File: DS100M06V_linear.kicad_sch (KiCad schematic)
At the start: 140 parts, among them J1 wire2board, J10 BNC_panel_mount, J11 wire2board, J2 Wire2Board, J3 wire2board, J4 wire2board, J5 Wire2Board, J6 Wire2Board, J7 Wire2Board, J8 red_safety_4mm_connector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

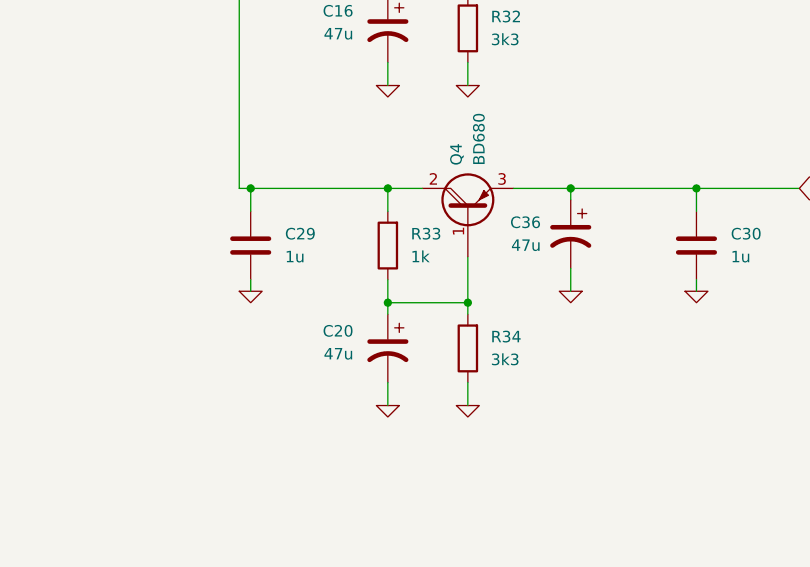
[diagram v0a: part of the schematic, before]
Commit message: Fixed electrolytics.
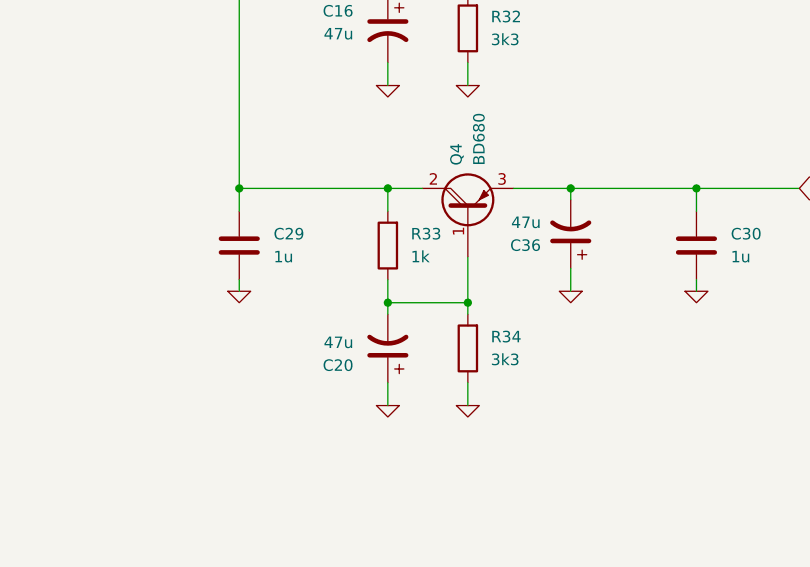
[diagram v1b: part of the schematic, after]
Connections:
- net -5V: now also C36.2; no longer C36.1
- net 0: now also C20.1, C36.1; no longer C20.2, C36.2
- net at Q4.1 (B), R33.1, R34.2: now also C20.2; no longer C20.1
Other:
- moved on the sheet: C20, C29, C36
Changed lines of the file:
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@@
 	)
 	(junction
-		(at 261.62 177.8)
+		(at 331.47 213.36)
 		(diameter 0)
 		(color 0 0 0 0)
 	)
 	(junction
-		(at 332.74 213.36)
+		(at 261.62 177.8)
 		(diameter 0)
 		(color 0 0 0 0)
@@
 	(wire
 		(pts
-			(xy 331.47 213.36) (xy 332.74 213.36)
+			(xy 331.47 213.36) (xy 347.98 213.36)
 		)
 		(stroke
@@
 	(wire
 		(pts
-			(xy 332.74 213.36) (xy 347.98 213.36)
-		)
-		(stroke
-			(width 0)
-			(type default)
-		)
-	)
-	(wire
-		(pts
 			(xy 368.3 189.23) (xy 368.3 186.69)
 		)
@@
 	(wire
 		(pts
-			(xy 332.74 224.79) (xy 332.74 223.52)
+			(xy 331.47 224.79) (xy 331.47 223.52)
 		)
 		(stroke
@@
 	(wire
 		(pts
-			(xy 332.74 213.36) (xy 332.74 215.9)
+			(xy 331.47 213.36) (xy 331.47 215.9)
 		)
 		(stroke
@@
 	(symbol
 		(lib_id "Device:C_Polarized_US")
-		(at 368.3 218.44 0)
-		(mirror y)
+		(at 368.3 218.44 180)
 		(unit 1)
 		(exclude_from_sim no)
@@
 		(dnp no)
 		(property "Reference" "C36"
-			(at 364.998 217.17 0)
+			(at 364.998 219.71 0)
 			(effects
 				(font
@@
 		)
 		(property "Value" "47u"
-			(at 364.998 219.71 0)
+			(at 364.998 217.17 0)
 			(effects
 				(font
@@
 	(symbol
 		(lib_id "Simulation_SPICE:0")
-		(at 332.74 224.79 0)
+		(at 331.47 224.79 0)
 		(unit 1)
 		(exclude_from_sim no)
@@
 		(fields_autoplaced yes)
 		(property "Reference" "#GND030"
-			(at 332.74 227.33 0)
+			(at 331.47 227.33 0)
 			(effects
 				(font
@@
 		)
 		(property "Value" "0"
-			(at 332.74 222.25 0)
+			(at 331.47 222.25 0)
 			(effects
 				(font
@@
 		)
 		(property "Footprint" ""
-			(at 332.74 224.79 0)
+			(at 331.47 224.79 0)
 			(effects
 				(font
@@
 		)
 		(property "Datasheet" "~"
-			(at 332.74 224.79 0)
+			(at 331.47 224.79 0)
 			(effects
 				(font
@@
 		)
 		(property "Description" ""
-			(at 332.74 224.79 0)
+			(at 331.47 224.79 0)
 			(effects
 				(font
@@
 	(symbol
 		(lib_id "Device:C")
-		(at 332.74 219.71 0)
+		(at 331.47 219.71 0)
 		(mirror y)
 		(unit 1)
@@
 		(fields_autoplaced yes)
 		(property "Reference" "C29"
-			(at 336.55 218.44 0)
+			(at 335.28 218.44 0)
 			(effects
 				(font
@@
 		)
 		(property "Value" "1u"
-			(at 336.55 220.98 0)
+			(at 335.28 220.98 0)
 			(effects
 				(font
@@
 		)
 		(property "Footprint" "Resistor_SMD:R_0603_1608Metric_Pad0.98x0.95mm_HandSolder"
-			(at 331.7748 223.52 0)
+			(at 330.5048 223.52 0)
 			(effects
 				(font
@@
 		)
 		(property "Datasheet" "~"
-			(at 332.74 219.71 0)
+			(at 331.47 219.71 0)
 			(effects
 				(font
@@
 		)
 		(property "Description" ""
-			(at 332.74 219.71 0)
+			(at 331.47 219.71 0)
 			(effects
 				(font
@@
 	(symbol
 		(lib_id "Device:C_Polarized_US")
-		(at 347.98 231.14 0)
-		(mirror y)
+		(at 347.98 231.14 180)
 		(unit 1)
 		(exclude_from_sim no)
@@
 		(on_board yes)
 		(dnp no)
-		(fields_autoplaced yes)
 		(property "Reference" "C20"
-			(at 344.17 229.2349 0)
+			(at 344.17 233.0451 0)
 			(effects
 				(font
@@
 		)
 		(property "Value" "47u"
-			(at 344.17 231.7749 0)
+			(at 344.17 230.5051 0)
 			(effects
 				(font

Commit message: Ferrites.
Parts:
- added FB1, FB2, FB3, FB4: FerriteBead, Inductor_SMD:L_0603_1608Metric_Pad1.05x0.95mm_HandSolder, symbol Device:FerriteBead
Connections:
- net +5V: now also FB2.2, FB4.2; no longer C19.2, C21.2, C26.2, C33.2, C34.2, C37.2, U1.8 (V+), U4.7 (V+)
- net -5V: now also FB1.2, FB3.2; no longer C18.2, C22.2, C25.2, C27.2, C35.2, C38.2, U1.4 (V-), U4.4 (V-)
- new net: C22.2, C25.2, C38.2, FB3.1, U4.4 (V-)
- new net: C21.2, C26.2, C37.2, FB4.1, U4.7 (V+)
- new net: C18.2, C27.2, C35.2, FB1.1, U1.4 (V-)
- new net: C19.2, C33.2, C34.2, FB2.1, U1.8 (V+)
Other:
- moved on the sheet: C18, C19, C22, C25, C27, C33, C34, C35, C38, H4
